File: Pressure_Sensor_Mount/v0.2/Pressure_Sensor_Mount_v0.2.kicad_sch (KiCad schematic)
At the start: 5 parts, among them J1 Conn_01x04_Pin

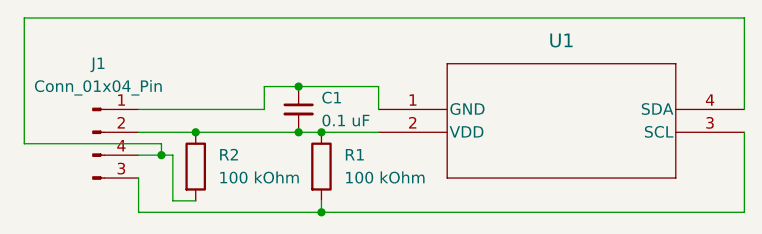
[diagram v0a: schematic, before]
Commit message: Uploaded new pressure sensor mount schematic and PCB
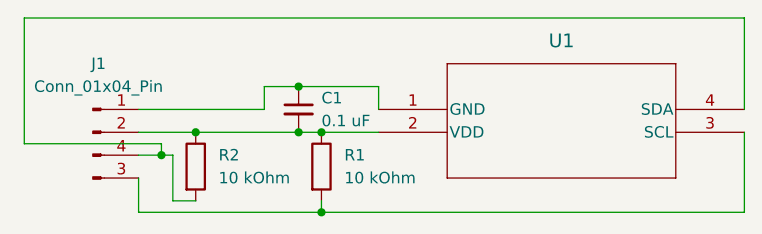
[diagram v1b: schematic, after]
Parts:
- C1: footprint (none) -> Capacitor_THT:C_Disc_D3.0mm_W1.6mm_P2.50mm
- R1, R2: value 100 kOhm -> 10 kOhm; footprint (none) -> Resistor_THT:R_Axial_DIN0309_L9.0mm_D3.2mm_P12.70mm_Horizontal
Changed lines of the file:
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@@
     (pin "4")
     (instances
-      (project "Pressure_Sensor_Mount"
+      (project "Pressure_Sensor_Mount_v0.2"
         (path "/36745fa6-eaa2-467e-b9f0-5e9a6d81871a"
           (reference "U1") (unit 1)
@@
     (pin "2")
     (instances
-      (project "Pressure_Sensor_Mount"
+      (project "Pressure_Sensor_Mount_v0.2"
         (path "/36745fa6-eaa2-467e-b9f0-5e9a6d81871a"
           (reference "J1") (unit 1)
@@
       (effects (font (size 1.27 1.27)) (justify left))
     )
-    (property "Footprint" "" (at 110.49 107.95 0)
+    (property "Footprint" "Capacitor_THT:C_Disc_D3.0mm_W1.6mm_P2.50mm" (at 110.49 107.95 0)
       (effects (font (size 1.27 1.27)) hide)
     )
@@
     (pin "2")
     (instances
-      (project "Pressure_Sensor_Mount"
+      (project "Pressure_Sensor_Mount_v0.2"
         (path "/36745fa6-eaa2-467e-b9f0-5e9a6d81871a"
           (reference "C1") (unit 1)
@@
       (effects (font (size 1.27 1.27)) (justify left))
     )
-    (property "Value" "100 kOhm" (at 101.6 115.57 0)
+    (property "Value" "10 kOhm" (at 101.6 115.57 0)
       (effects (font (size 1.27 1.27)) (justify left))
     )
-    (property "Footprint" "" (at 97.282 114.3 90)
+    (property "Footprint" "Resistor_THT:R_Axial_DIN0309_L9.0mm_D3.2mm_P12.70mm_Horizontal" (at 97.282 114.3 90)
       (effects (font (size 1.27 1.27)) hide)
     )
@@
     (pin "1")
     (instances
-      (project "Pressure_Sensor_Mount"
+      (project "Pressure_Sensor_Mount_v0.2"
         (path "/36745fa6-eaa2-467e-b9f0-5e9a6d81871a"
           (reference "R2") (unit 1)
@@
       (effects (font (size 1.27 1.27)) (justify left))
     )
-    (property "Value" "100 kOhm" (at 115.57 115.57 0)
+    (property "Value" "10 kOhm" (at 115.57 115.57 0)
       (effects (font (size 1.27 1.27)) (justify left))
     )
-    (property "Footprint" "" (at 111.252 114.3 90)
+    (property "Footprint" "Resistor_THT:R_Axial_DIN0309_L9.0mm_D3.2mm_P12.70mm_Horizontal" (at 111.252 114.3 90)
       (effects (font (size 1.27 1.27)) hide)
     )
@@
     (pin "1")
     (instances
-      (project "Pressure_Sensor_Mount"
+      (project "Pressure_Sensor_Mount_v0.2"
         (path "/36745fa6-eaa2-467e-b9f0-5e9a6d81871a"
           (reference "R1") (unit 1)
